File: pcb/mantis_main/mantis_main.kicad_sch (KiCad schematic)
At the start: 114 parts, among them J3 nice!nano extra, J4 Pin Header, J5 JST-PH, J6 Conn_01x02_Socket, M1 SW_Mouse, M2 SW_Mouse, SW1 SW_SPDT, U1 74LVC1G17

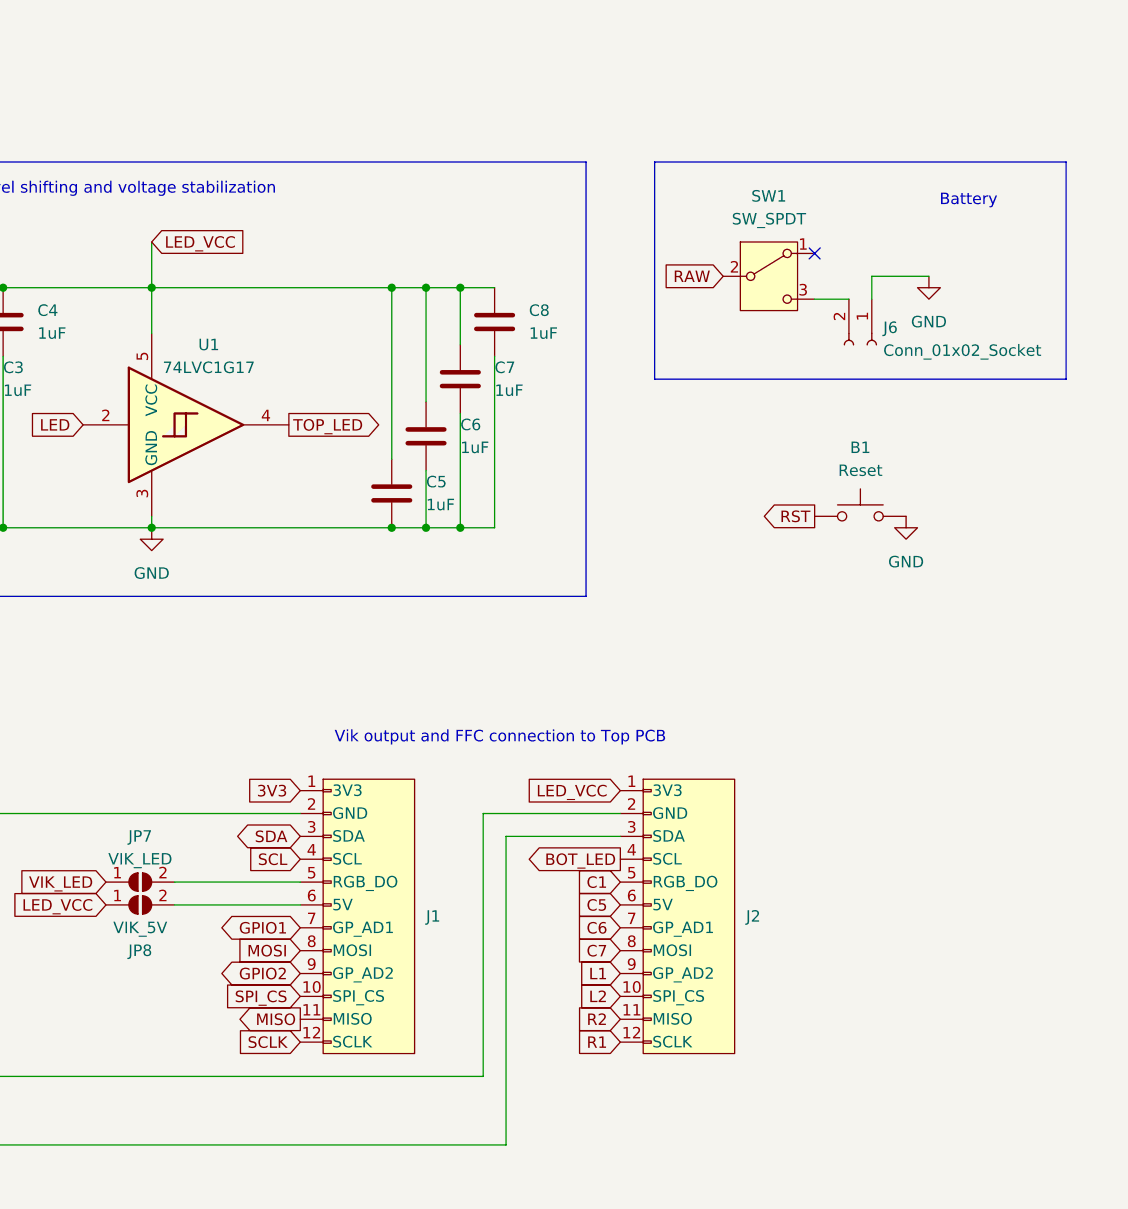
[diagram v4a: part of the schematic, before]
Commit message: pcb: Update mantis_main schematic
Added second battery connector that can be placed with 180° rotation to
support batteries with different polarity.

Added named nets for BAT and VIK_5V so I can assign a "Power" netclass to
them.

Signed-off-by: Felix Kuehling <felix.kuehling@gmail.com>
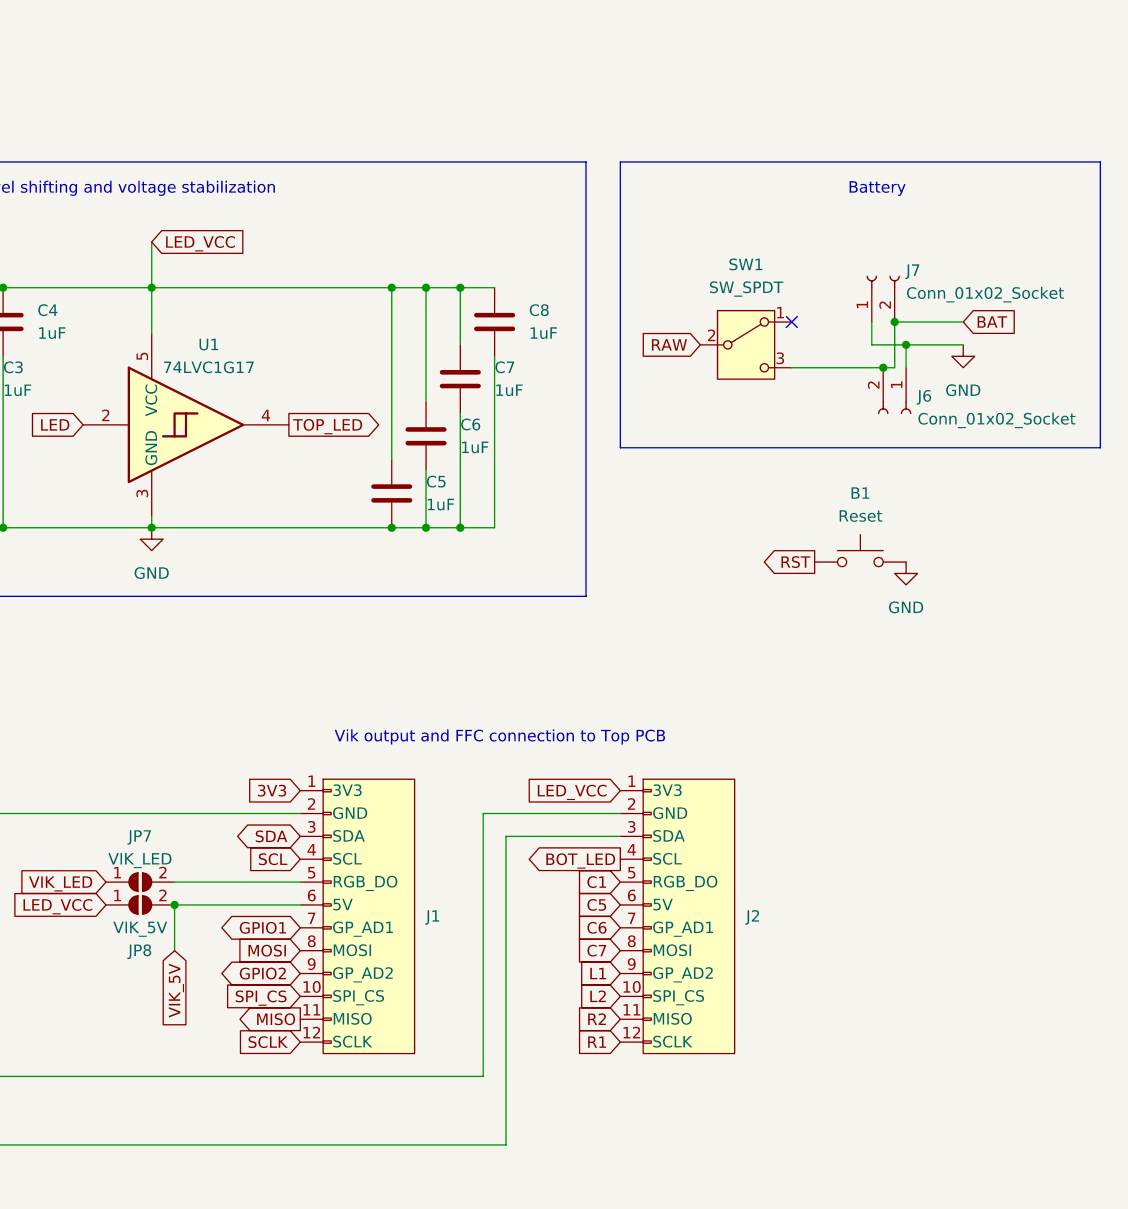
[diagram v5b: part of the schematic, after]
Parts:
- added J7: Conn_01x02_Socket, Connector_JST:JST_PH_S2B-PH-K_1x02_P2.00mm_Horizontal, symbol Connector:Conn_01x02_Socket
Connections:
- net GND: now also J7.1 (Pin_1)
- net VIK_5V: now reaches J1.6 (5V), JP8.2 (B)
- net BAT: now reaches J6.2 (Pin_2), SW1.3 (C)
- net BAT: now also J7.2 (Pin_2)
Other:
- moved on the sheet: B1, J6, SW1

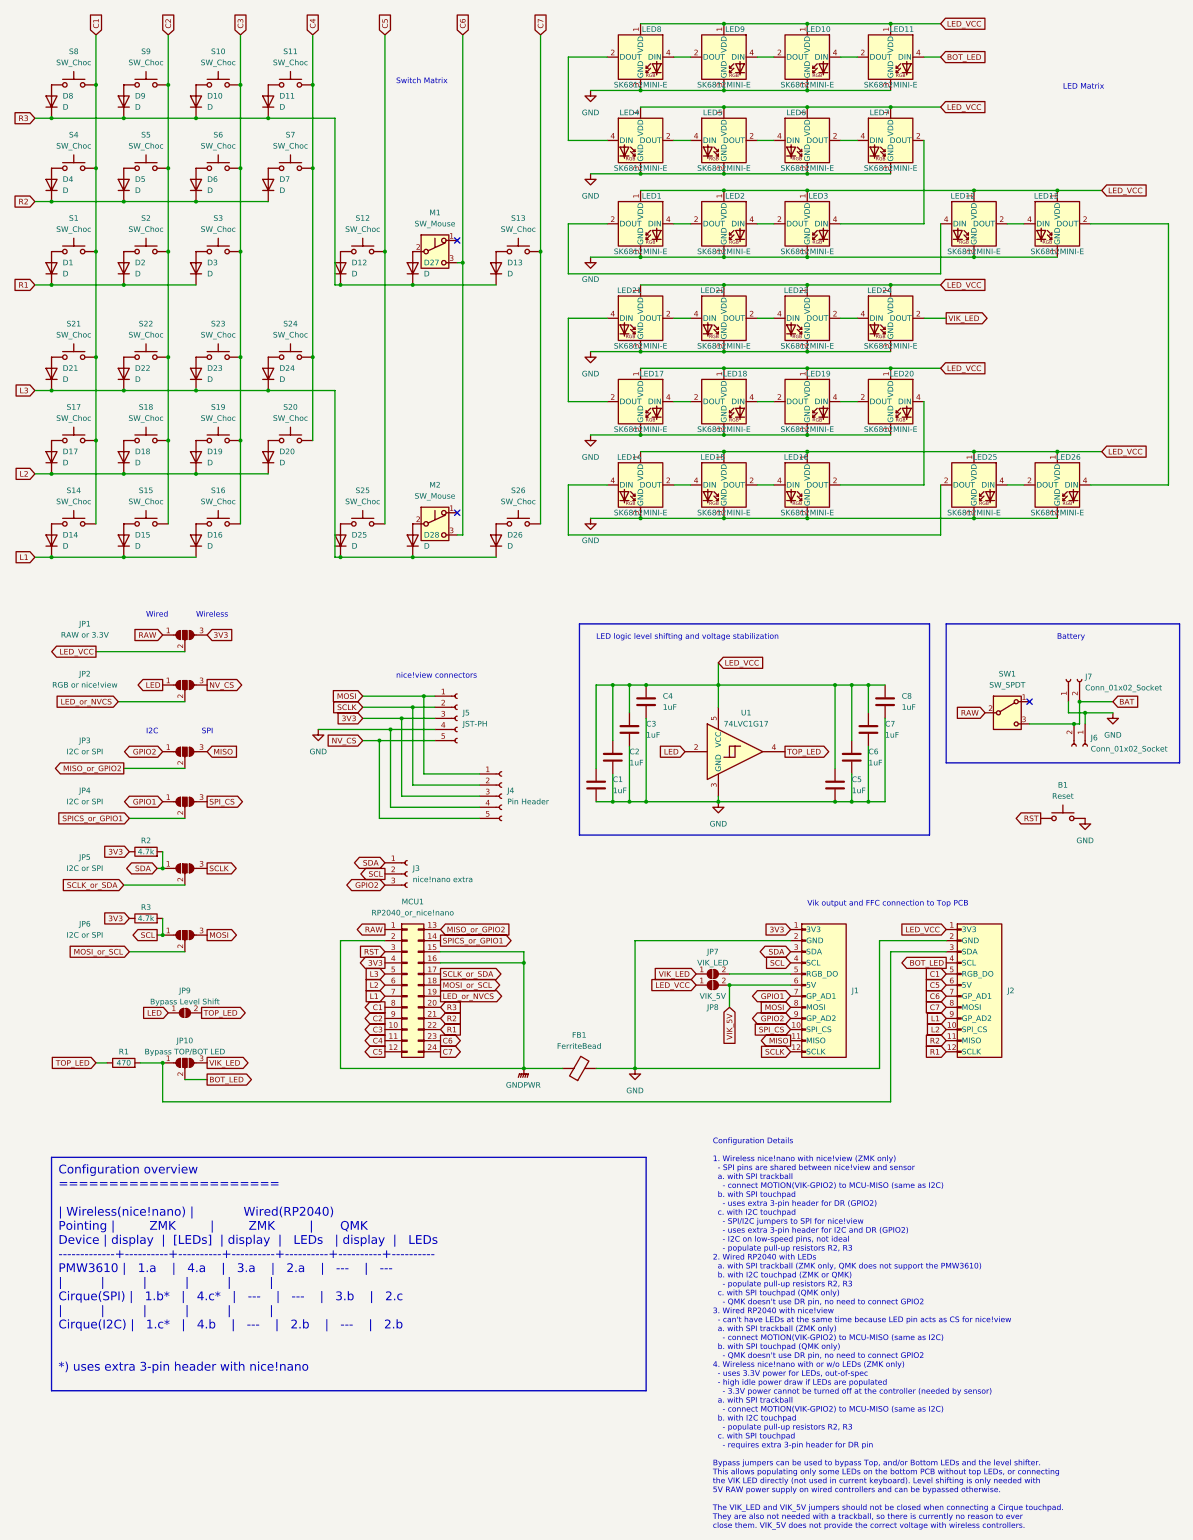
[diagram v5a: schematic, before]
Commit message: pcb/mantis_main: Fixes and tweaks
Corrected the matrix to match Ergogen: 3 bottom row keys use C2, C3, C4.
C1 keeps one extra spot for the raised PCB.

Added jumper to bypass the ferrite bead.

Repositioned ferrite bead to give it more solid GND connection.

Minor position tweaks for battery switch, and display connector.

Many routing improvements, more ground vias.

Added Mantis graphic, VIK logo and signature.

Signed-off-by: Felix Kuehling <felix.kuehling@gmail.com>
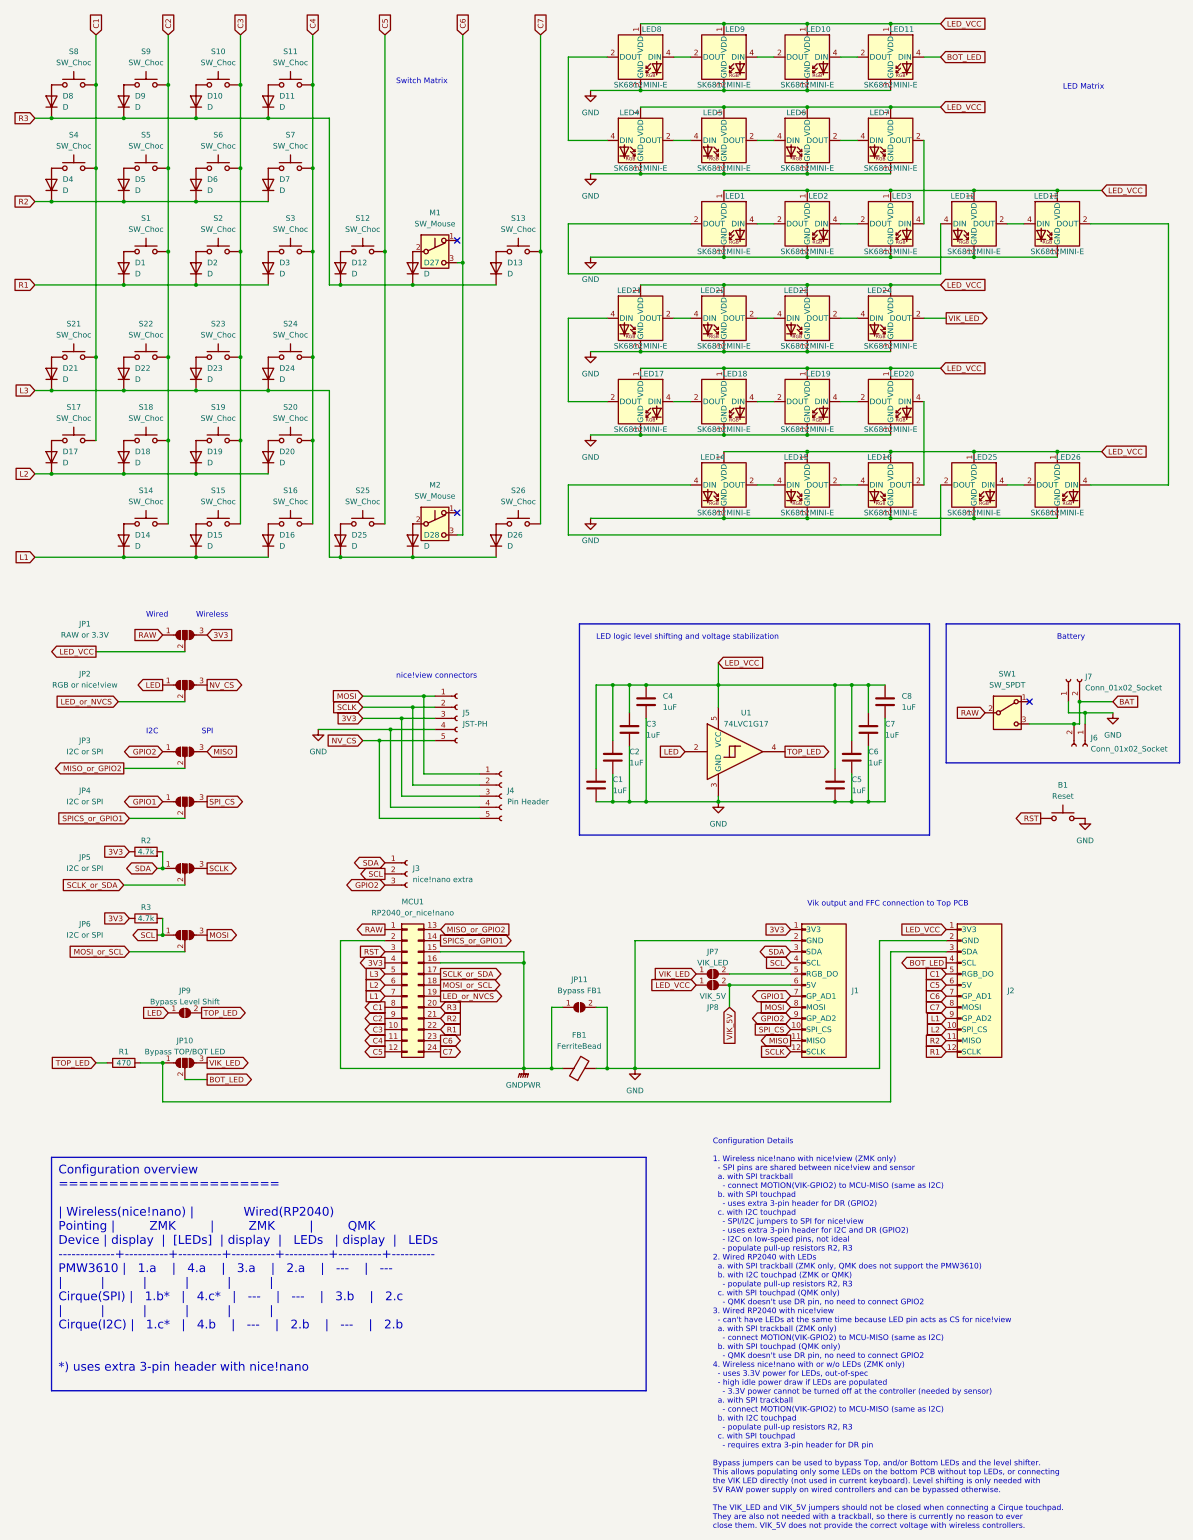
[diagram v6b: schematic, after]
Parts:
- added JP11: Bypass FB1, Jumper:SolderJumper-2_P1.3mm_Open_RoundedPad1.0x1.5mm, symbol Jumper:SolderJumper_2_Open
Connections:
- net C1: no longer S1.2, S14.2
- net C2: now also S1.2, S14.2; no longer S15.2, S2.2
- net C3: now also S15.2, S2.2; no longer S16.2, S3.2
- net C4: now also S16.2, S3.2
- net GND: now also JP11.2 (B)
- net GNDPWR: now also JP11.1 (A)
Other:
- moved on the sheet: D1, D14, D15, D16, D2, D3, LED1, LED14, LED15, LED16, LED2, LED3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

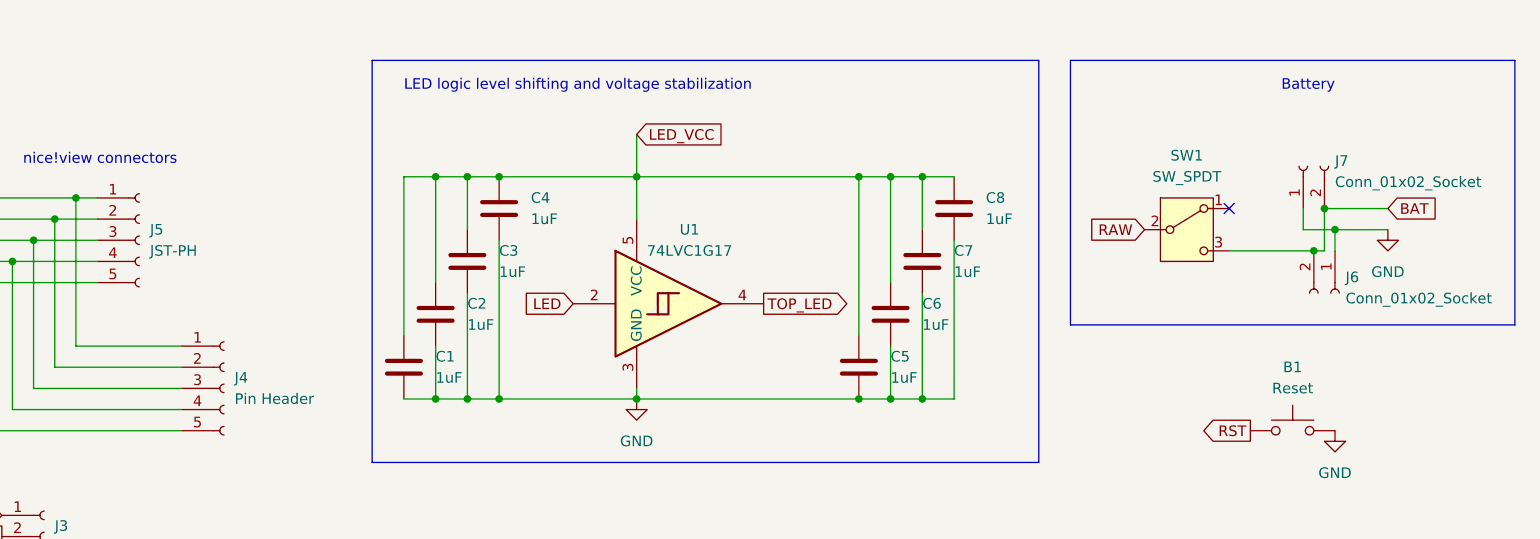
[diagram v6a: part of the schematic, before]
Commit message: pcb: Reposition battery connector
Renumbered connectors to match updated ergogen, which now includes the
battery connector. Removed second battery connector again.

Updated PCB and routing to wire up the connector in the new location and
take advantage of the freed-up real-estate under the controller.

Signed-off-by: Felix Kuehling <felix.kuehling@gmail.com>
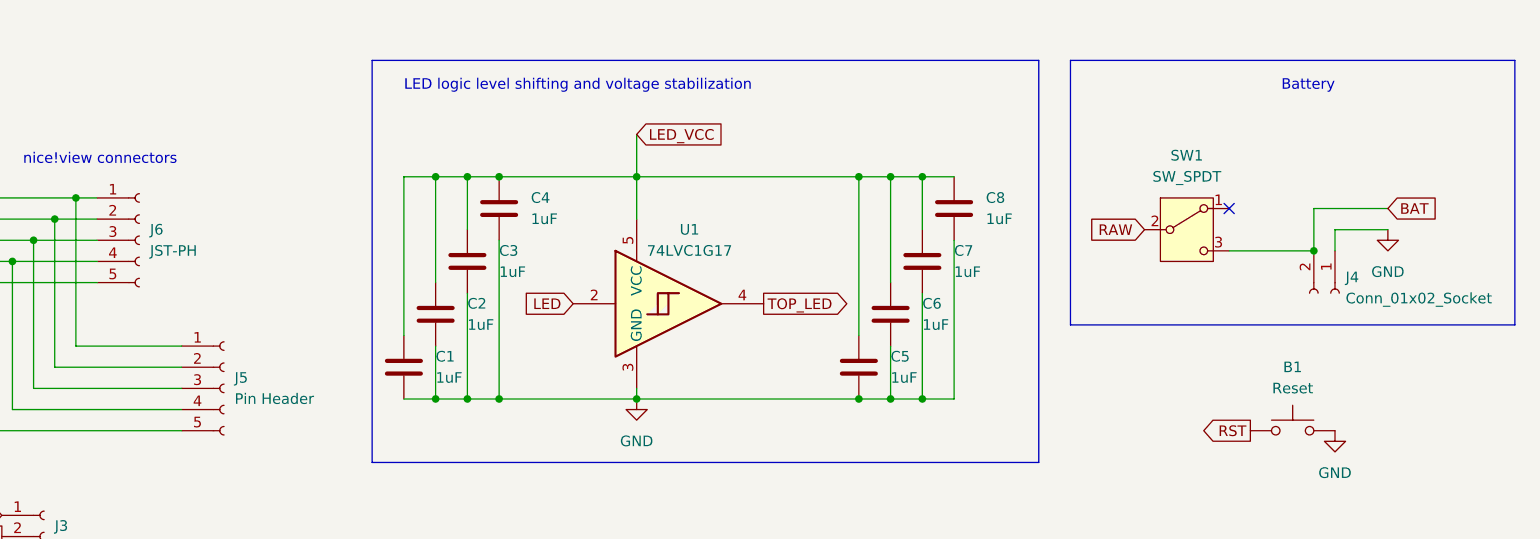
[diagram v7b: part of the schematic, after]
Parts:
- removed J7: Conn_01x02_Socket, Connector_JST:JST_PH_S2B-PH-K_1x02_P2.00mm_Horizontal, symbol Connector:Conn_01x02_Socket
- renumbered J6 to J4, J4 to J5, J5 to J6
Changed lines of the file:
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@@
   (junction (at 81.28 111.76) (diameter 0) (color 0 0 0 0)
   )
-  (junction (at 256.54 171.45) (diameter 0) (color 0 0 0 0)
-  )
   (junction (at 64.77 111.76) (diameter 0) (color 0 0 0 0)
   )
@@
   (junction (at 64.77 30.48) (diameter 0) (color 0 0 0 0)
   )
-  (junction (at 257.81 173.99) (diameter 0) (color 0 0 0 0)
-  )
   (no_connect (at 114.3 66.04))
   (no_connect (at 114.3 128.27))
@@
     (stroke (width 0) (type default))
   )
-  (wire (pts (xy 257.81 173.99) (xy 254 173.99))
-    (stroke (width 0) (type default))
-  )
   (wire (pts (xy 163.83 102.87) (xy 167.64 102.87))
     (stroke (width 0) (type default))
@@
     (stroke (width 0) (type default))
   )
-  (wire (pts (xy 255.27 176.53) (xy 256.54 176.53))
-    (stroke (width 0) (type default))
-  )
   (wire (pts (xy 139.7 83.82) (xy 148.59 83.82))
     (stroke (width 0) (type default))
@@
     (stroke (width 0) (type default))
   )
-  (wire (pts (xy 254 171.45) (xy 254 173.99))
-    (stroke (width 0) (type default))
-  )
   (wire (pts (xy 146.05 186.69) (xy 146.05 167.64))
     (stroke (width 0) (type default))
@@
     (stroke (width 0) (type default))
   )
-  (wire (pts (xy 256.54 176.53) (xy 256.54 171.45))
+  (wire (pts (xy 255.27 176.53) (xy 255.27 171.45))
     (stroke (width 0) (type default))
   )
@@
     (stroke (width 0) (type default))
   )
-  (wire (pts (xy 256.54 171.45) (xy 264.16 171.45))
+  (wire (pts (xy 255.27 171.45) (xy 264.16 171.45))
     (stroke (width 0) (type default))
   )
@@
     )
   )
-  (symbol (lib_id "Connector:Conn_01x02_Socket") (at 254 166.37 90) (unit 1)
-    (in_bom yes) (on_board yes) (dnp no) (fields_autoplaced)
-    (property "Reference" "J7" (at 257.81 165.735 90)
-      (effects (font (size 1.27 1.27)) (justify right))
-    )
-    (property "Value" "Conn_01x02_Socket" (at 257.81 168.275 90)
-      (effects (font (size 1.27 1.27)) (justify right))
-    )
-    (property "Footprint" "Connector_JST:JST_PH_S2B-PH-K_1x02_P2.00mm_Horizontal" (at 254 166.37 0)
-      (effects (font (size 1.27 1.27)) hide)
-    )
-    (property "Datasheet" "~" (at 254 166.37 0)
-      (effects (font (size 1.27 1.27)) hide)
-    )
-    (pin "1")
-    (pin "2")
-    (instances
-      (project "mantis_main"
-        (path "/39b0d399-e3dd-4da0-86c3-d024b50c6a59"
-          (reference "J7") (unit 1)
-        )
-      )
-    )
-  )
   (symbol (lib_id "Mantis:SK6812MINI-E") (at 194.31 121.92 0) (mirror y) (unit 1)
     (in_bom yes) (on_board yes) (dnp no)
@@
   (symbol (lib_id "Connector:Conn_01x05_Socket") (at 114.3 175.26 0) (unit 1)
     (in_bom yes) (on_board yes) (dnp no) (fields_autoplaced)
-    (property "Reference" "J5" (at 115.57 173.99 0)
+    (property "Reference" "J6" (at 115.57 173.99 0)
       (effects (font (size 1.27 1.27)) (justify left))
     )
@@
       (project "mantis_main"
         (path "/39b0d399-e3dd-4da0-86c3-d024b50c6a59"
-          (reference "J5") (unit 1)
+          (reference "J6") (unit 1)
         )
       )
@@
   (symbol (lib_id "Connector:Conn_01x02_Socket") (at 257.81 181.61 270) (unit 1)
     (in_bom yes) (on_board yes) (dnp no) (fields_autoplaced)
-    (property "Reference" "J6" (at 259.08 179.705 90)
+    (property "Reference" "J4" (at 259.08 179.705 90)
       (effects (font (size 1.27 1.27)) (justify left))
     )
@@
       (project "mantis_main"
         (path "/39b0d399-e3dd-4da0-86c3-d024b50c6a59"
-          (reference "J6") (unit 1)
+          (reference "J4") (unit 1)
         )
       )
@@
   (symbol (lib_id "Connector:Conn_01x05_Socket") (at 124.46 193.04 0) (unit 1)
     (in_bom yes) (on_board yes) (dnp no) (fields_autoplaced)
-    (property "Reference" "J4" (at 125.73 191.77 0)
+    (property "Reference" "J5" (at 125.73 191.77 0)
       (effects (font (size 1.27 1.27)) (justify left))
     )
@@
       (project "mantis_main"
         (path "/39b0d399-e3dd-4da0-86c3-d024b50c6a59"
-          (reference "J4") (unit 1)
+          (reference "J5") (unit 1)
         )
       )
